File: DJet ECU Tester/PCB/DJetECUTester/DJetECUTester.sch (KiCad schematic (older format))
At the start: 39 parts, among them J1 ISP, J10 ECU3, J2 ECU1, J4 12V 4A IN (5.5/2.5), J5 12V IN, J6 MPS, J7 Conn_01x01, J8 Conn_01x01, J9 ECU2, M1 Fan_3pin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

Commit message: Added screw block for connecting ECU power switch.
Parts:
- removed J7, J8: Conn_01x01, Britishideas:tabconnector-63849-1, symbol Connector_Generic:Conn_01x01
- added J7: ECU PWR SWITCH, Britishideas:PhoenixContact_COMBICON_MKDSN_2, symbol Connector:Screw_Terminal_01x02
- M1: manf# (none) -> 22-23-2031
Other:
- note removed: "ECU power switch"
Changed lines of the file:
@@
 Wire Wire Line
 	9150 1950 9150 2100
-$Comp
-L Connector_Generic:Conn_01x01 J7
-U 1 1 63367628
-P 9400 2400
-F 0 "J7" V 9500 2450 50  0000 R CNN
-F 1 "Conn_01x01" V 9273 2312 50  0001 R CNN
-F 2 "Britishideas:tabconnector-63849-1" H 9400 2400 50  0001 C CNN
-F 3 "~" H 9400 2400 50  0001 C CNN
-F 4 "63849-1" V 9400 2400 50  0001 C CNN "manf#"
-	1    9400 2400
-	0    -1   -1   0
-$EndComp
-$Comp
-L Connector_Generic:Conn_01x01 J8
-U 1 1 63367D5E
-P 9600 2400
-F 0 "J8" V 9700 2450 50  0000 R CNN
-F 1 "Conn_01x01" V 9473 2312 50  0001 R CNN
-F 2 "Britishideas:tabconnector-63849-1" H 9600 2400 50  0001 C CNN
-F 3 "~" H 9600 2400 50  0001 C CNN
-F 4 "63849-1" V 9600 2400 50  0001 C CNN "manf#"
-	1    9600 2400
-	0    -1   -1   0
-$EndComp
 Wire Wire Line
 	9150 2600 9400 2600
 Connection ~ 9150 2600
 Wire Wire Line
-	9600 2600 10000 2600
-Wire Wire Line
 	10000 2600 10000 2800
 Connection ~ 10000 2800
-Text Notes 9250 2250 0    50   ~ 0
-ECU power switch
 Text Label 10150 2600 0    50   ~ 0
 ECU_PWR
@@
 F 2 "Connector:FanPinHeader_1x03_P2.54mm_Vertical" H 4700 5110 50  0001 C CNN
 F 3 "http://www.hardwarecanucks.com/forum/attachments/new-builds/16287d1330775095-help-chassis-power-fan-connectors-motherboard-asus_p8z68.jpg" H 4700 5110 50  0001 C CNN
+F 4 "22-23-2031" H 4700 5200 50  0001 C CNN "manf#"
 	1    4700 5200
 	1    0    0    -1
 $EndComp
+$Comp
+L Connector:Screw_Terminal_01x02 J7
+U 1 1 634C4439
+P 9400 2400
+F 0 "J7" V 9400 2150 50  0000 L CNN
+F 1 "ECU PWR SWITCH" V 9500 1950 50  0000 L CNN
+F 2 "Britishideas:PhoenixContact_COMBICON_MKDSN_2" H 9400 2400 50  0001 C CNN
+F 3 "~" H 9400 2400 50  0001 C CNN
+F 4 "1729018" H 9400 2400 50  0001 C CNN "manf#"
+	1    9400 2400
+	0    -1   -1   0
+$EndComp
+Wire Wire Line
+	9500 2600 10000 2600
 $EndSCHEMATC

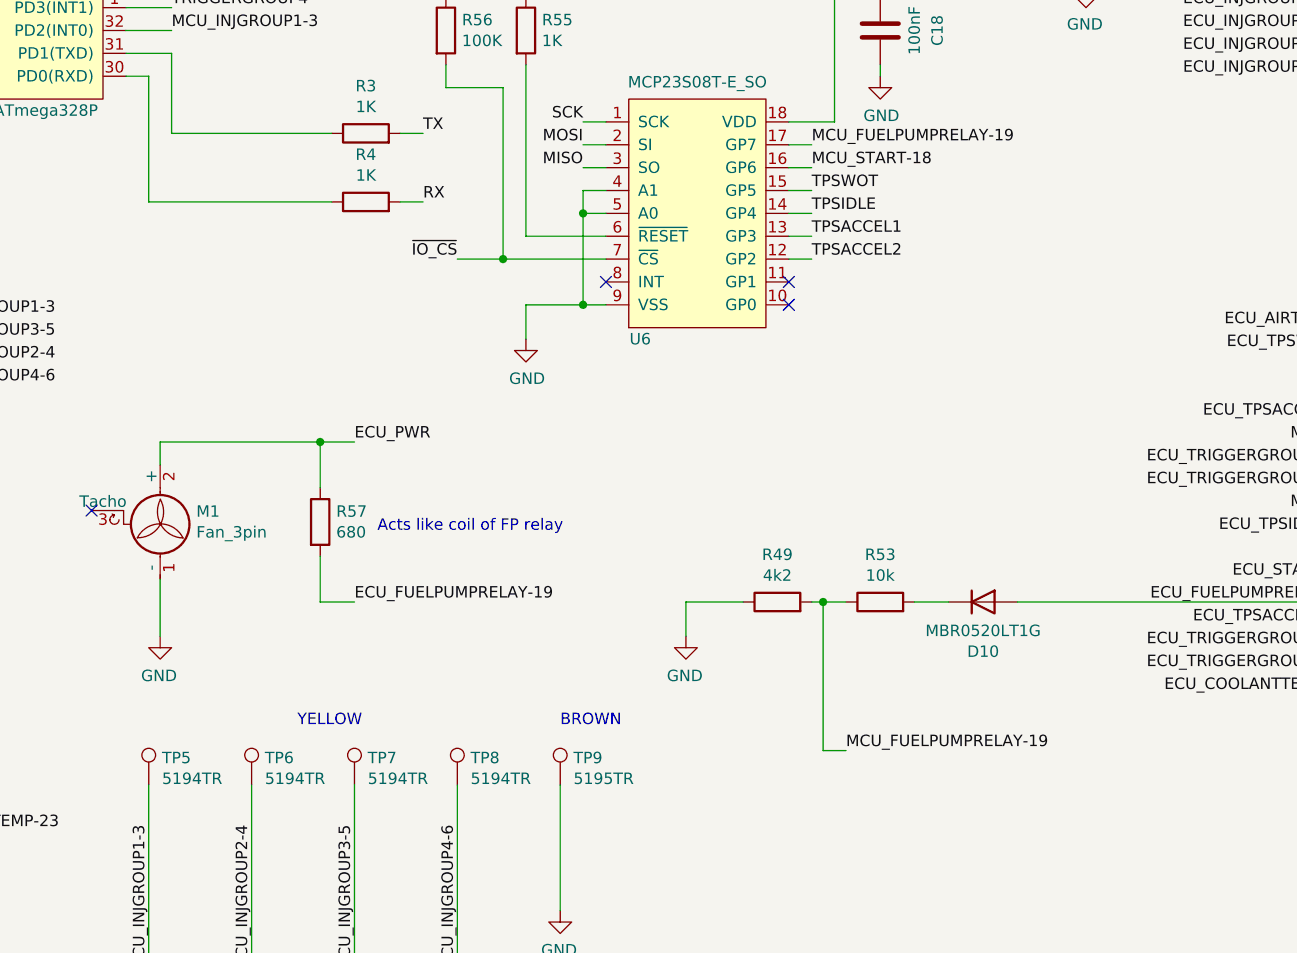
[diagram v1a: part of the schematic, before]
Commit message: Added more robust test points. Added GPIO connector.
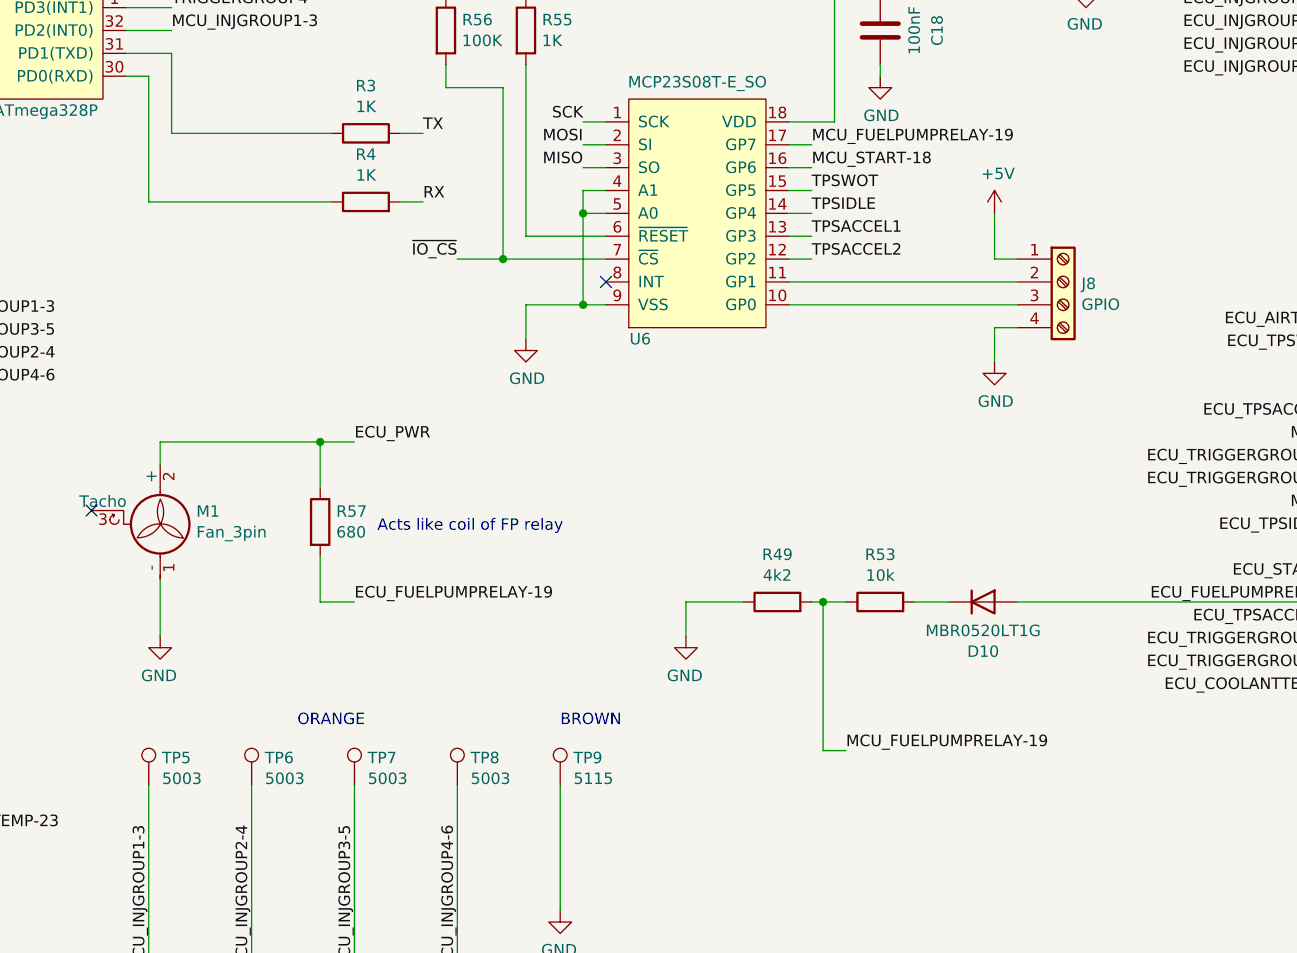
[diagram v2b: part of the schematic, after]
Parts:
- added J8: GPIO, Britishideas:PhoenixContact_COMBICON_PT_4, symbol Connector:Screw_Terminal_01x04
- TP5, TP6, TP7, TP8: value 5194TR -> 5003; footprint Britishideas:5190TR-Colored-Test-Point -> Britishideas:Keystone-Minature-Test-Point-Colored-500x-511x
- TP9: value 5195TR -> 5115; footprint Britishideas:5190TR-Colored-Test-Point -> Britishideas:Keystone-Minature-Test-Point-Colored-500x-511x
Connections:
- net +5V: now also J8.1 (Pin_1)
- net GND: now also J8.4 (Pin_4)
- net at U6.10 (GP0): now also J8.3 (Pin_3)
- net at U6.11 (GP1): now also J8.2 (Pin_2)
- no-connect marks 8 -> 6
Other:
- note added: "ORANGE"
- note removed: "YELLOW"
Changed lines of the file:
@@
 P 4650 6400
 F 0 "TP5" H 4708 6518 50  0000 L CNN
-F 1 "5194TR" H 4708 6427 50  0000 L CNN
-F 2 "Britishideas:5190TR-Colored-Test-Point" H 4850 6400 50  0001 C CNN
+F 1 "5003" H 4708 6427 50  0000 L CNN
+F 2 "Britishideas:Keystone-Minature-Test-Point-Colored-500x-511x" H 4850 6400 50  0001 C CNN
 F 3 "~" H 4850 6400 50  0001 C CNN
 F 4 "5194TR" H 4650 6400 50  0001 C CNN "manf#"
@@
 P 5100 6400
 F 0 "TP6" H 5158 6518 50  0000 L CNN
-F 1 "5194TR" H 5158 6427 50  0000 L CNN
-F 2 "Britishideas:5190TR-Colored-Test-Point" H 5300 6400 50  0001 C CNN
+F 1 "5003" H 5158 6427 50  0000 L CNN
+F 2 "Britishideas:Keystone-Minature-Test-Point-Colored-500x-511x" H 5300 6400 50  0001 C CNN
 F 3 "~" H 5300 6400 50  0001 C CNN
 F 4 "5194TR" H 5100 6400 50  0001 C CNN "manf#"
@@
 P 5550 6400
 F 0 "TP7" H 5608 6518 50  0000 L CNN
-F 1 "5194TR" H 5608 6427 50  0000 L CNN
-F 2 "Britishideas:5190TR-Colored-Test-Point" H 5750 6400 50  0001 C CNN
+F 1 "5003" H 5608 6427 50  0000 L CNN
+F 2 "Britishideas:Keystone-Minature-Test-Point-Colored-500x-511x" H 5750 6400 50  0001 C CNN
 F 3 "~" H 5750 6400 50  0001 C CNN
 F 4 "5194TR" H 5550 6400 50  0001 C CNN "manf#"
@@
 P 6000 6400
 F 0 "TP8" H 6058 6518 50  0000 L CNN
-F 1 "5194TR" H 6058 6427 50  0000 L CNN
-F 2 "Britishideas:5190TR-Colored-Test-Point" H 6200 6400 50  0001 C CNN
+F 1 "5003" H 6058 6427 50  0000 L CNN
+F 2 "Britishideas:Keystone-Minature-Test-Point-Colored-500x-511x" H 6200 6400 50  0001 C CNN
 F 3 "~" H 6200 6400 50  0001 C CNN
 F 4 "5194TR" H 6000 6400 50  0001 C CNN "manf#"
@@
 P 6450 6400
 F 0 "TP9" H 6508 6518 50  0000 L CNN
-F 1 "5195TR" H 6508 6427 50  0000 L CNN
-F 2 "Britishideas:5190TR-Colored-Test-Point" H 6650 6400 50  0001 C CNN
+F 1 "5115" H 6508 6427 50  0000 L CNN
+F 2 "Britishideas:Keystone-Minature-Test-Point-Colored-500x-511x" H 6650 6400 50  0001 C CNN
 F 3 "~" H 6650 6400 50  0001 C CNN
 F 4 "5195TR" H 6450 6400 50  0001 C CNN "manf#"
@@
 BROWN
 Text Notes 5300 6150 0    50   ~ 0
-YELLOW
+ORANGE
 Wire Wire Line
 	4650 6400 4650 7200
@@
 ~IO_CS
 NoConn ~ 4550 2400
-NoConn ~ 7450 4300
 Text Label 4750 1900 0    50   ~ 0
 ~COOLANTTEMP2_CS
@@
 Wire Wire Line
 	10100 5500 9900 5500
-NoConn ~ 7450 4200
 $Sheet
 S 1700 3800 1400 200
@@
 Wire Wire Line
 	9500 2600 10000 2600
+$Comp
+L Connector:Screw_Terminal_01x04 J8
+U 1 1 634FDA44
+P 8650 4200
+F 0 "J8" H 8730 4192 50  0000 L CNN
+F 1 "GPIO" H 8730 4101 50  0000 L CNN
+F 2 "Britishideas:PhoenixContact_COMBICON_PT_4" H 8650 4200 50  0001 C CNN
+F 3 "~" H 8650 4200 50  0001 C CNN
+F 4 "1935792" H 8650 4200 50  0001 C CNN "manf#"
+F 5 "1935187" H 8650 4200 50  0001 C CNN "manf2#"
+	1    8650 4200
+	1    0    0    -1
+$EndComp
+Wire Wire Line
+	7450 4300 8450 4300
+Wire Wire Line
+	7450 4200 8450 4200
+$Comp
+L power:GND #PWR079
+U 1 1 6351D4E8
+P 8350 4550
+F 0 "#PWR079" H 8350 4300 50  0001 C CNN
+F 1 "GND" H 8355 4377 50  0000 C CNN
+F 2 "" H 8350 4550 50  0001 C CNN
+F 3 "" H 8350 4550 50  0001 C CNN
+	1    8350 4550
+	1    0    0    -1
+$EndComp
+Wire Wire Line
+	8350 4550 8350 4400
+Wire Wire Line
+	8350 4400 8450 4400
+$Comp
+L power:+5V #PWR078
+U 1 1 6352C90A
+P 8350 3900
+F 0 "#PWR078" H 8350 3750 50  0001 C CNN
+F 1 "+5V" H 8365 4073 50  0000 C CNN
+F 2 "" H 8350 3900 50  0001 C CNN
+F 3 "" H 8350 3900 50  0001 C CNN
+	1    8350 3900
+	1    0    0    -1
+$EndComp
+Wire Wire Line
+	8350 3900 8350 4100
+Wire Wire Line
+	8350 4100 8450 4100
 $EndSCHEMATC

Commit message: Updated symbols from rescue to library.
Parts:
- M1: symbol BritishIdeas:Fan_3pin -> DJetECUTester-rescue:Fan_3pin-BritishIdeas
- U1: symbol BritishIdeas:ATmega328P -> DJetECUTester-rescue:ATmega328P-BritishIdeas
- U6: symbol BritishIdeas:MCP23S08T-E_SO -> DJetECUTester-rescue:MCP23S08T-E_SO-BritishIdeas
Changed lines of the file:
@@
 $EndDescr
 $Comp
-L BritishIdeas:ATmega328P U1
+L DJetECUTester-rescue:ATmega328P-BritishIdeas U1
 U 1 1 5FE91942
 P 3000 3400
@@
 NoConn ~ 10100 6100
 $Comp
-L BritishIdeas:MCP23S08T-E_SO U6
+L DJetECUTester-rescue:MCP23S08T-E_SO-BritishIdeas U6
 U 1 1 6328F4DE
 P 6750 4400
@@
 NoConn ~ 4400 5200
 $Comp
-L BritishIdeas:Fan_3pin M1
+L DJetECUTester-rescue:Fan_3pin-BritishIdeas M1
 U 1 1 63504226
 P 4700 5200
